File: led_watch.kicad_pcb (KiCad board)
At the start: 4 copper layers, 29 x 29 mm, 95 parts, among them U3 M0G3507QDGS32RQ1, Y2 TXC-7C

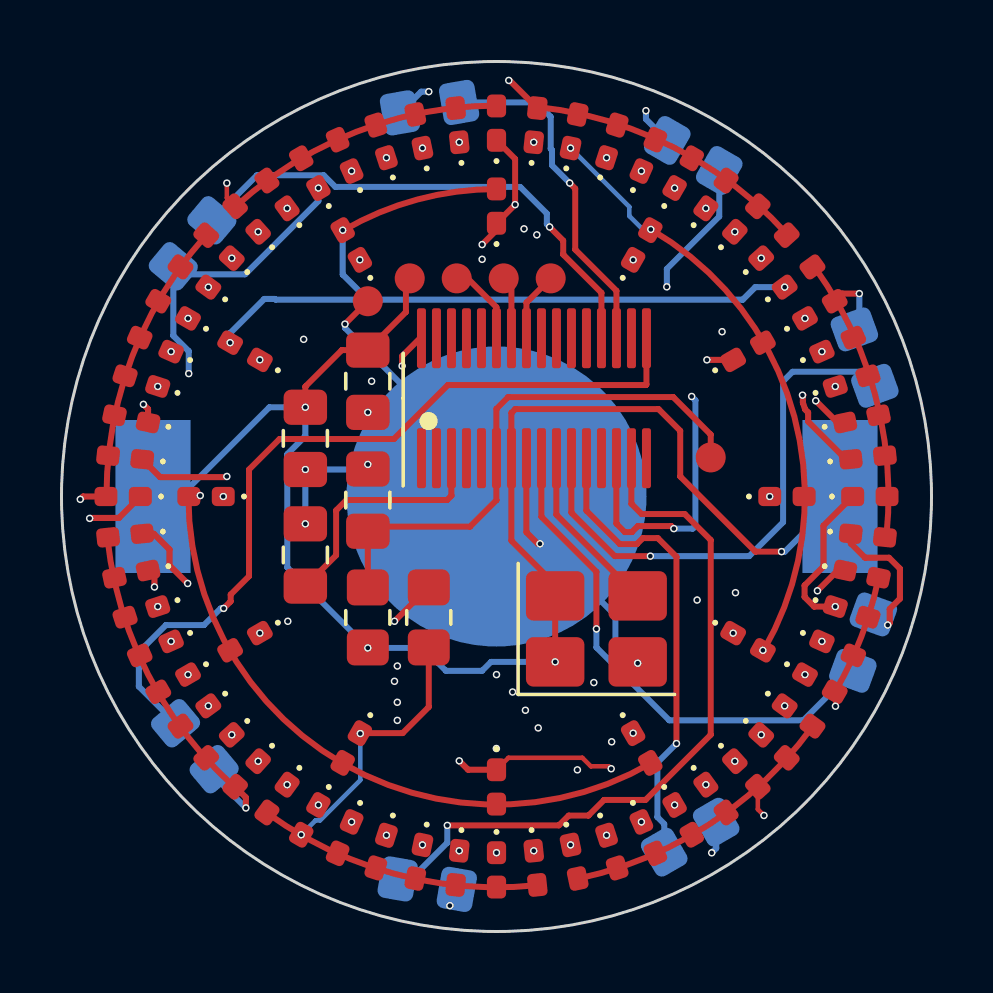
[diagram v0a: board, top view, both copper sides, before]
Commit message: add button
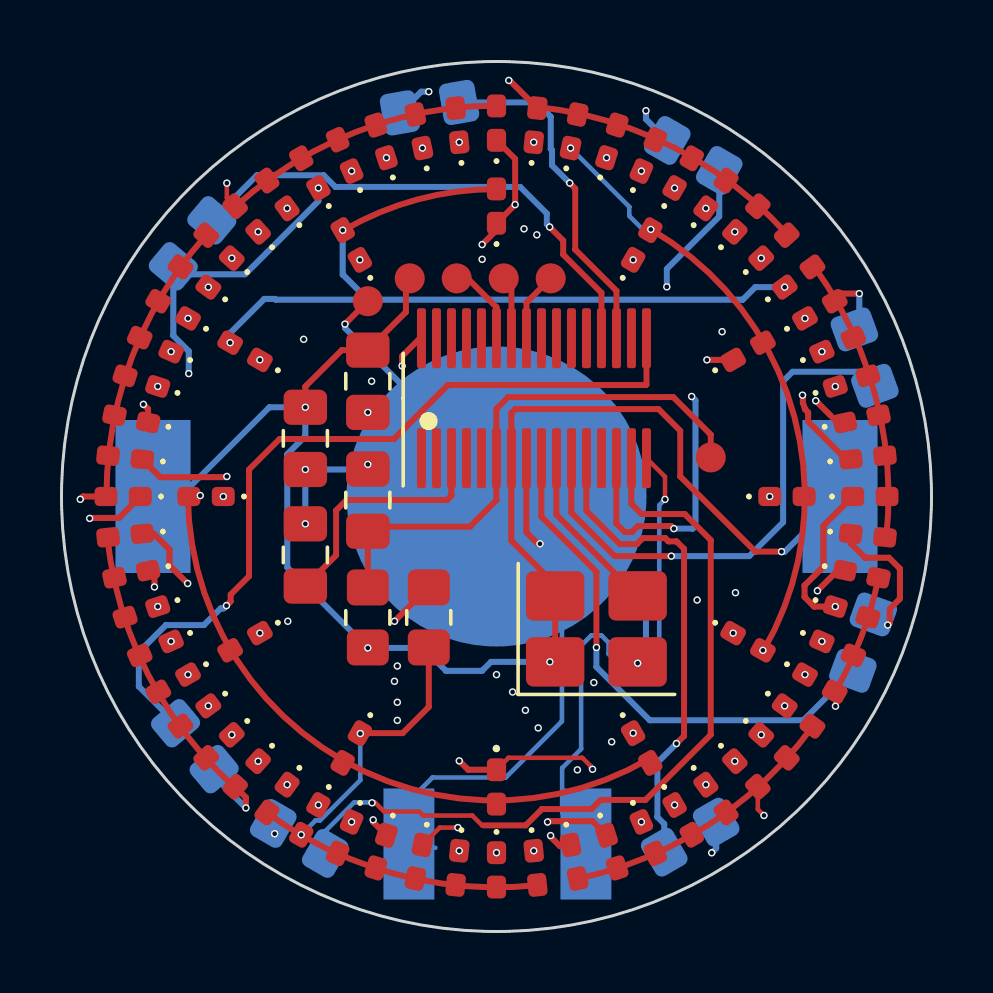
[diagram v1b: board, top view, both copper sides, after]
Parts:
- added S1: KSS223GLFG, led_watch:KSS223GLFG, B.Cu at (107.2, 64.3)
- moved R7 4.53 mm to (100.6, 63.6), turned to 150 degrees
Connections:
- U3 pad 16: unconnected-(U3-PA9/RTC_OUT/CLK_OUT-Pad16) -> Net-(U3-PA9/RTC_OUT/CLK_OUT)
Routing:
- net Net-(U3-PA9/RTC_OUT/CLK_OUT): track 0.00 -> 18.3 mm, vias 0 -> 1
- net GND: track 28.1 -> 46.0 mm
- net PA10: track 82.2 -> 85.4 mm
- net Net-(U3-PA8): track 23.9 -> 26.9 mm
- net PA8/SPI0_CS0: track 87.7 -> 85.1 mm
- net Net-(U3-PA5/HFXIN/FCC_IN): track 15.8 -> 16.3 mm
